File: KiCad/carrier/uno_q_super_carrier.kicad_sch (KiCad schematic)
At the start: 0 parts

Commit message: Rebuild all schematics as valid KiCad 10 format (version 20260326)
Complete rewrite from scratch using Python generator (kicad10_gen.py).
All 16 files verified parseable with kicad-skip and structurally
compliant with the KiCad schematic file format specification.

Format compliance per dev-docs.kicad.org/en/file-formats/sexpr-schematic/:
  - version 20260326 (KiCad 10 SEXPR_SCHEMATIC_FILE_VERSION)
  - generator_version 10.0.0
  - Root (uuid) in every schematic file header
  - Every symbol instance has: (uuid UUID) + (instances (project NAME (path /ROOT/SHEET (reference REF)(unit N))))
  - Every hierarchical_label has: (uuid UUID)
  - Every sheet block has: (uuid UUID) + (instances (project NAME (path /ROOT_UUID (page N))))
  - Every sheet pin has: (uuid UUID)
  - Every text element has: (uuid UUID)
  - Root schematics have: (sheet_instances (path '/' (page '1')))
  - lib_symbols: pin type uses 'TYPE line' format (e.g. 'input line')
  - All property effects use correct KiCad 10 token syntax
  - Stable UUIDs via seed files (shield_uuids.json, carrier_uuids.json)

Shield (8 files, stable root UUID: bc84562d-846a-4607-81a1-500b7991d137):
  uno_q_hub75_shield.kicad_sch      root, 7 hierarchical sheets
  sheets/power.kicad_sch            AMS1117-3.3 LDO, FB1, indicators (17 syms)
  sheets/esp32s3.kicad_sch          ESP32-S3-WROOM-1-N16R8, USB-C (9 syms)
  sheets/hub75_driver.kicad_sch     SN74HCT245PW x2, HUB75 IDC (10 syms)
  sheets/audio_codec.kicad_sch      ES8388, DC-block caps, J_OUT/J_MIC (19 syms)
  sheets/display.kicad_sch          FPC_22pin, GT911 pullups, JP1 (7 syms)
  sheets/uno_q_interface.kicad_sch  J2 SPI3, J3 UART debug (2 syms)
  sheets/connectivity.kicad_sch     Qwiic x2, Grove x5 (10 syms)

Carrier (8 files, stable root UUID: a7d62ed3-8e95-4e64-b6df-722c91664a1a):
  uno_q_super_carrier.kicad_sch     root, 10 hierarchical sheets
  sheets/power.kicad_sch            TPS54331DR buck, AMS1117, dual VIN/HUB75 (33 syms)
  sheets/uno_q_mounting.kicad_sch   B1 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
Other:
- sheet ESP32-S3 ports: added CS_S3_MPU; removed none
- note added: "UNO Q SUPER CARRIER — Rev 0.1 — BLOCK DIAGRAM\n\nSignal flow (IEEE 315: left→right power top→bottom):\n\n J_VIN(7-24V) → [POWER] → +5V(TPS54331) +3V3(AMS1117)\n J_HUB(5V) → [POWER] → +5V_HUB75 (panel direct)\n B1/B2(JMISC/JMEDIA) → [UNO Q MOUNTING] → SPI/I2C/MIPI/GPIO\n [MOUNTING] → SPI → [ESP32-S3] + [ESP32-C6]\n [ESP32-S3] → UART → [ESP32-C6] (direct independent of UNO Q)\n [ESP32-S3] → HUB75 G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"
- note removed: "UNO Q SUPER CARRIER — Rev 0.1 — BLOCK DIAGRAM Signal flow (IEEE 315: left→right, power top→bottom): J_VIN (7-24V) ──> [POWER] ──> +5V (TPS54331 buck), +3V3 (AMS1117) J_HUB (5V) ──> [POWER] ──> +5V_HUB75 (direct to panel) B1/B2 (JMISC/JMEDIA) ──> [UNO Q MOUNTING] ──> SPI/I2C/MIPI/GPIO [UNO Q MOUNTING] ──> SPI ──> [ESP32-S3] + [ESP32-C6] [ESP32-S3] ──> HUB75 GPIO ──> [HUB75 DRIVER] ──> panel IDC [E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"

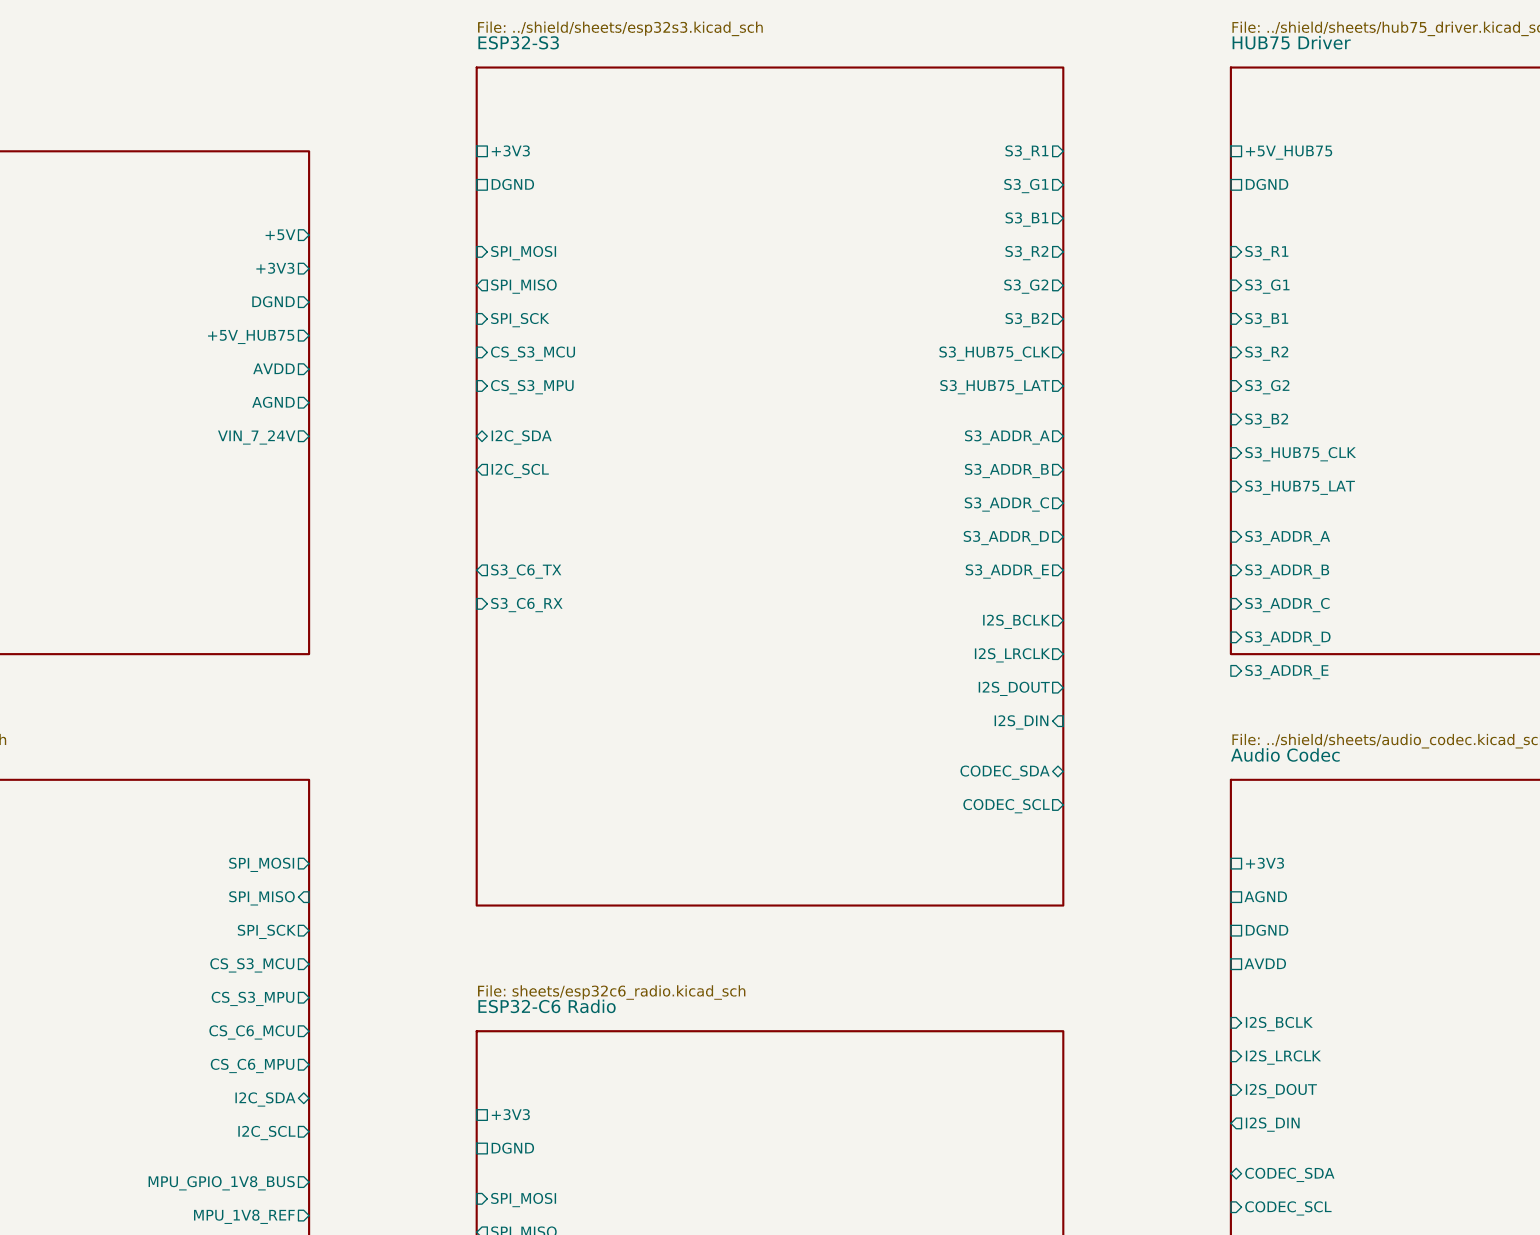
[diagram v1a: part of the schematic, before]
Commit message: Fix hierarchy mismatches — all 16 files fully audited and clean
Issues found and fixed by full-depth structural audit:

1. esp32s3.kicad_sch (shared sheet used by both boards):
   Missing 3 carrier-specific hierarchical labels:
     + CS_S3_MPU (GPIO0, carrier-only QRB2210 chip select)
     + S3_C6_TX  (S3→C6 direct UART, carrier-only)
     + S3_C6_RX  (C6→S3, carrier-only)
   These labels are valid in the shield context too (NC at shield level)
   Shield root + carrier root now both declare all 37 pins correctly

2. carrier/uno_q_super_carrier.kicad_sch (root):
   esp32s3 sheet block: missing LCD_*/TOUCH_INT pins (7 pins)
   These were declared in the shield root but dropped from carrier root
   All 37 pins now declared, matching all 37 hierarchical labels exactly

3. Net name mismatch: '+5V_HUB75' vs '+5V_EXT_HUB75'
   carrier/sheets/power.kicad_sch label: +5V_HUB75 → +5V_EXT_HUB75
   Now matches HUB75 driver sheet and carrier root declaration

Final audit results (full-depth parenthesis parsing, not window-based):
  16/16 files pass all structural checks:
  version 20260326, generator_version 10.0.0, header uuid,
  sheet_instances with path '/', symbol instances (uuid+instances),
  hierarchical_labels (uuid), sheet blocks (uuid+instances),
  sheet pins (uuid), text elements (uuid), lib pin 'TYPE line' format,
  zero duplicate UUIDs, all 17 sheet hierarchy pin↔label pairs match exactly
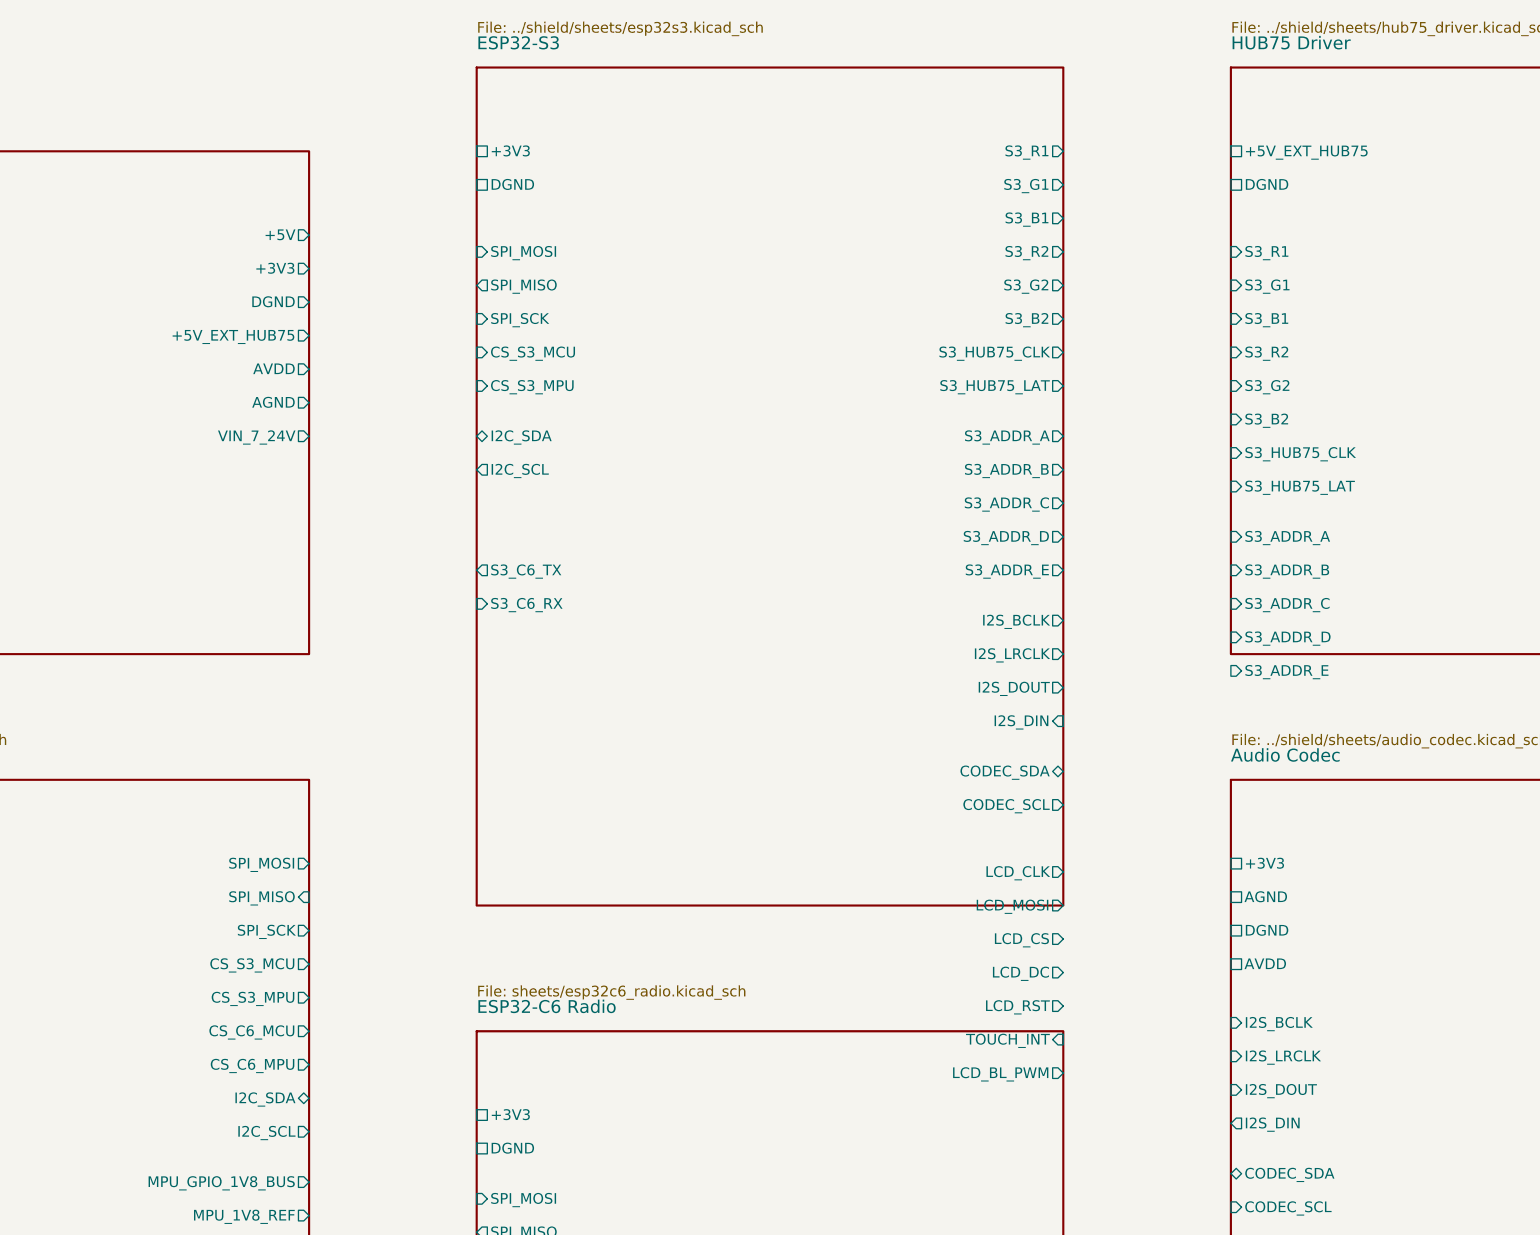
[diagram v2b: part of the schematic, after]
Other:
- sheet ESP32-S3 ports: added LCD_BL_PWM, LCD_CLK, LCD_CS, LCD_DC, LCD_MOSI, LCD_RST, TOUCH_INT; removed none
- sheet HUB75 Driver ports: added +5V_EXT_HUB75; removed +5V_HUB75
- sheet Power ports: added +5V_EXT_HUB75; removed +5V_HUB75
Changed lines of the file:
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@@
       (effects (font (size 1.27 1.27)))
     )
-    (pin "+5V_HUB75" output
+    (pin "+5V_EXT_HUB75" output
       (at 90 52 0)
       (effects (font (size 1.27 1.27)))
@@
       (effects (font (size 1.27 1.27)))
     )
-    (instances
+        (pin "LCD_CLK" output
+      (at 180 116 0)
+      (effects (font (size 1.27 1.27)))
+    )
+    (pin "LCD_MOSI" output
+      (at 180 120 0)
+      (effects (font (size 1.27 1.27)))
+    )
+    (pin "LCD_CS" output
+      (at 180 124 0)
+      (effects (font (size 1.27 1.27)))
+    )
+    (pin "LCD_DC" output
+      (at 180 128 0)
+      (effects (font (size 1.27 1.27)))
+    )
+    (pin "LCD_RST" output
+      (at 180 132 0)
+      (effects (font (size 1.27 1.27)))
+    )
+    (pin "TOUCH_INT" input
+      (at 180 136 0)
+      (effects (font (size 1.27 1.27)))
+    )
+    (pin "LCD_BL_PWM" output
+      (at 180 140 0)
+      (effects (font (size 1.27 1.27)))
+    )
+(instances
       (project "uno_q_super_carrier"
         (path "/a7d62ed3-8e95-4e64-b6df-722c91664a1a"
@@
       (effects (font (size 1.27 1.27)) (justify left bottom))
     )
-    (pin "+5V_HUB75" power_in
+    (pin "+5V_EXT_HUB75" power_in
       (at 200 30 180)
       (effects (font (size 1.27 1.27)))
